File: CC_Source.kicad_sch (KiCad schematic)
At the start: 14 parts, among them Q10301 IRLML5103, U10302 ADA4807-1

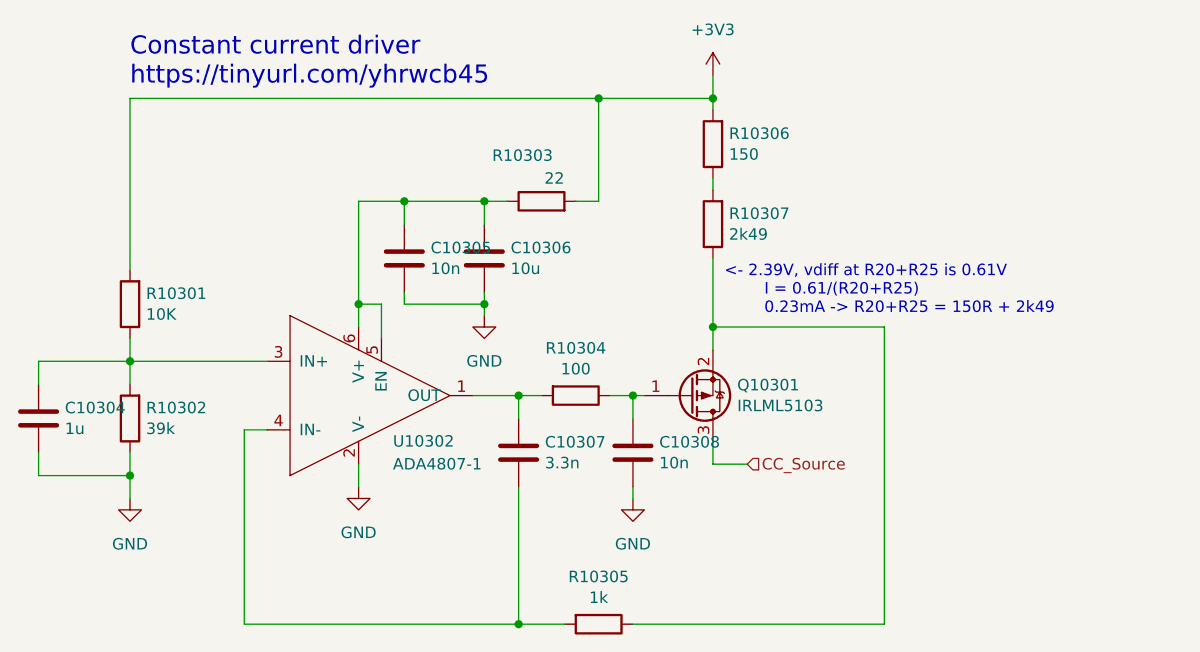
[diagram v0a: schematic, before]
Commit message: restructurization of the entire project improved
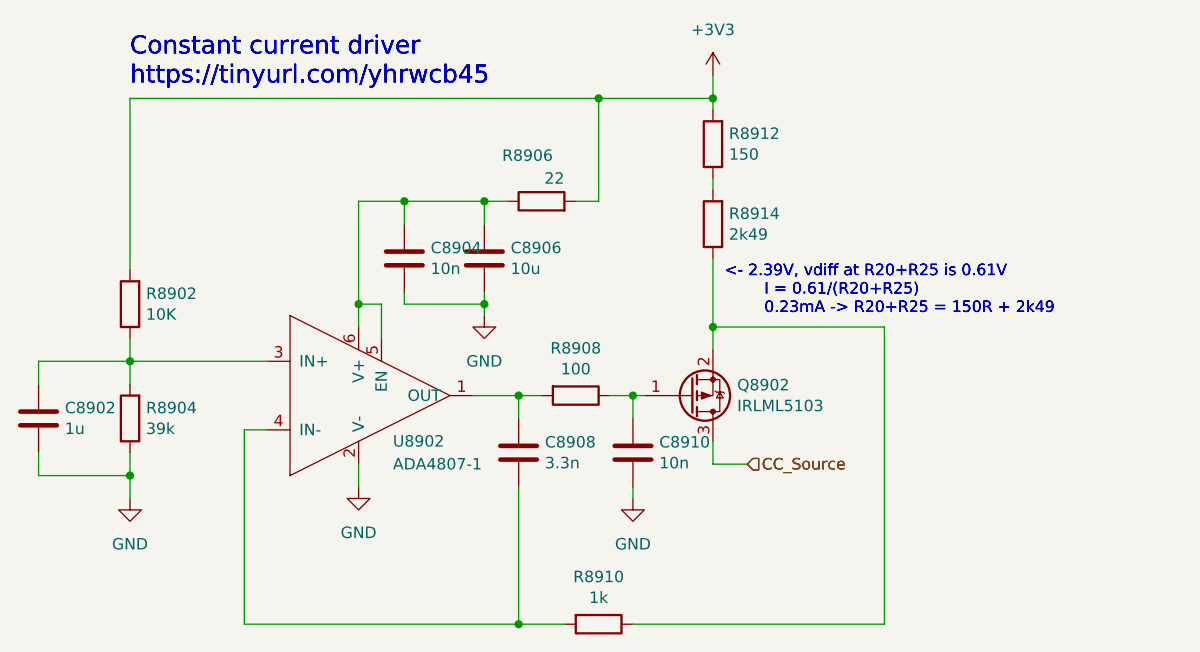
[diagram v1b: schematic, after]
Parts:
- removed C10304: 1u, Capacitor_SMD:C_0603_1608Metric_Pad1.08x0.95mm_HandSolder, symbol Device:C
- removed C10307: 3.3n, Capacitor_SMD:C_0603_1608Metric_Pad1.08x0.95mm_HandSolder, symbol Device:C
- removed R10301: 10K, Resistor_SMD:R_0603_1608Metric, symbol Device:R
- removed R10304: 100, Resistor_SMD:R_0603_1608Metric, symbol Device:R
- removed U10302: ADA4807-1, Package_TO_SOT_SMD:SOT-363_SC-70-6, symbol vzlu_lib:AD8029
- added C8902: 1u, Capacitor_SMD:C_0603_1608Metric_Pad1.08x0.95mm_HandSolder, symbol Device:C
- added C8908: 3.3n, Capacitor_SMD:C_0603_1608Metric_Pad1.08x0.95mm_HandSolder, symbol Device:C
- added R8902: 10K, Resistor_SMD:R_0603_1608Metric, symbol Device:R
- added R8908: 100, Resistor_SMD:R_0603_1608Metric, symbol Device:R
- added U8902: ADA4807-1, Package_TO_SOT_SMD:SOT-363_SC-70-6, symbol vzlu_lib:AD8029
- renumbered C10305 to C8904, C10306 to C8906, C10308 to C8910, Q10301 to Q8902, R10302 to R8904, R10303 to R8906, R10305 to R8910, R10306 to R8912, R10307 to R8914
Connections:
- net +3V3: now also R8902.2
- net GND: now also C8902.2, U8902.2 (V-)
- net at R8904.2: now also C8902.1, R8902.1, U8902.3 (IN+)
- net at R8910.2: now also C8908.2, U8902.4 (IN-)
- net at C8904.1, C8906.1, R8906.1: now also U8902.5 (EN), U8902.6 (V+)
- net at C8910.1, Q8902.1 (G): now also R8908.1
- new net: C8908.1, R8908.2, U8902.1 (OUT)
